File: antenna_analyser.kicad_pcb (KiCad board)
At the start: 2 copper layers, 88.9 x 53.3 mm, 25 parts, among them IC1 MCP6002, P1 CONN_01X10, P2 CONN_01X10, P3 CONN_01X04, P4 CONN_01X02

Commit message: Updates to the schematic.
Replaced 50ohm and 5kohm resistors with their equivalent parallel circuits.
Added an AD9850 module to the schematic for easier reference.
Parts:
- removed C1: 1uF, Capacitors_Elko_ThroughHole:Elko_vert_20x10mm_RM2.5
- removed C2, C4: 100n, Capacitors_ThroughHole:C_Disc_D3_P2.5
- removed C3, C5, C6: 10n, Capacitors_ThroughHole:C_Disc_D3_P2.5
- removed D1, D2: AA143, Diodes_ThroughHole:Diode_DO-41_SOD81_Horizontal_RM10
- removed IC1: MCP6002, Housings_SSOP:MSOP-8_3x3mm_Pitch0.65mm
- removed P1, P2: CONN_01X10, Pin_Headers:Pin_Header_Straight_1x10
- removed P3: CONN_01X04, Pin_Headers:Pin_Header_Straight_1x04
- removed P4: CONN_01X02, Pin_Headers:Pin_Header_Straight_1x02
- removed R1, R2, R3: 50, Resistors_ThroughHole:Resistor_Horizontal_RM10mm
- removed R10, R6: 5k, Resistors_ThroughHole:Resistor_Horizontal_RM10mm
- removed R11, R7: 648, Resistors_ThroughHole:Resistor_Horizontal_RM10mm
- removed R4, R8: 10k, Resistors_ThroughHole:Resistor_Horizontal_RM10mm
- removed R5, R9: 100k, Resistors_ThroughHole:Resistor_Horizontal_RM10mm
- removed SMA_E1: SMA_EDGE, sma:SMA
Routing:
- removed copper zone on B.Cu, net GND
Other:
- board outline removed

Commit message: PCB first attempt, no luck. Need to make sure the elements are on the correct side.
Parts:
- added C1: 1uF, Capacitors_Elko_ThroughHole:Elko_vert_20x10mm_RM2.5, F.Cu at (126.4, 108.0)
- added C2: 100n, Capacitors_ThroughHole:C_Disc_D3_P2.5, F.Cu at (162.6, 83.2)
- added C3: 10n, Capacitors_ThroughHole:C_Disc_D3_P2.5, F.Cu at (162.6, 79.4)
- added C4: 100n, Capacitors_ThroughHole:C_Disc_D3_P2.5, F.Cu at (144.1, 117.5)
- added C5: 10n, Capacitors_ThroughHole:C_Disc_D3_P2.5, F.Cu at (144.1, 120.7)
- added C6: 10n, Capacitors_ThroughHole:C_Disc_D3_P2.5, F.Cu at (92.1, 90.2)
- added D1: AA143, Diodes_ThroughHole:Diode_DO-41_SOD81_Horizontal_RM10, F.Cu at (168.3, 93.3)
- added D2: AA143, Diodes_ThroughHole:Diode_DO-41_SOD81_Horizontal_RM10, F.Cu at (168.3, 96.5)
- added ENC1: BI_EN11-HSM1AF15, Rotary-Encoders:BI_EN12-HS22AF30, F.Cu at (172.7, 113.7)
- added IC1: MCP6002, sop8:SOP-8, F.Cu at (143.5, 80.0)
- added IC2: ARDUINO_PRO_MINI_5V, arduino pro mini:ARDUINO_PRO_MINI, F.Cu at (149.2, 98.4)
- added P1: AD9850_CONN, dds-module-ad9850:DDS_AD9850, F.Cu at (109.9, 97.8)
- added P2: CONN_LCD, Pin_Headers:Pin_Header_Straight_1x15, F.Cu at (83.8, 81.9)
- added R1: 100, Resistors_ThroughHole:Resistor_Horizontal_RM10mm, F.Cu at (156.2, 101.6)
- added R10: 100, Resistors_ThroughHole:Resistor_Horizontal_RM10mm, F.Cu at (130.2, 88.3)
- added R11: 648, Resistors_ThroughHole:Resistor_Horizontal_RM10mm, F.Cu at (173.4, 78.1)
- added R12: 100, Resistors_ThroughHole:Resistor_Horizontal_RM10mm, F.Cu at (127.0, 88.3)
- added R13: 10k, Resistors_ThroughHole:Resistor_Horizontal_RM10mm, F.Cu at (94.6, 81.9)
- added R14: 10k, Resistors_ThroughHole:Resistor_Horizontal_RM10mm, F.Cu at (91.4, 81.9)
- added R15: 10k, Resistors_ThroughHole:Resistor_Horizontal_RM10mm, F.Cu at (88.3, 81.9)
- added R16: 10k, Resistors_ThroughHole:Resistor_Horizontal_RM10mm, F.Cu at (88.3, 95.2)
- added R2: 100, Resistors_ThroughHole:Resistor_Horizontal_RM10mm, F.Cu at (173.4, 87.0)
- added R3: 100, Resistors_ThroughHole:Resistor_Horizontal_RM10mm, F.Cu at (156.2, 88.3)
- added R4: 10k, Resistors_ThroughHole:Resistor_Horizontal_RM10mm, F.Cu at (173.4, 90.2)
- added R5: 100k, Resistors_ThroughHole:Resistor_Horizontal_RM10mm, F.Cu at (173.4, 83.8)
- added R6: 100, Resistors_ThroughHole:Resistor_Horizontal_RM10mm, F.Cu at (173.4, 99.7)
- added R7: 648, Resistors_ThroughHole:Resistor_Horizontal_RM10mm, F.Cu at (173.4, 80.6)
- added R8: 10k, Resistors_ThroughHole:Resistor_Horizontal_RM10mm, F.Cu at (133.3, 113.0)
- added R9: 100k, Resistors_ThroughHole:Resistor_Horizontal_RM10mm, F.Cu at (133.3, 88.3)
- added SMA_E1: SMA_EDGE, SMA_EDGE:SMA_EDGE, F.Cu at (128.3, 69.2)
- added U1: AMS1117, SOT223:SOT223, F.Cu at (130.2, 100.3)
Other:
- board outline added: 99.7 x 50.8 mm

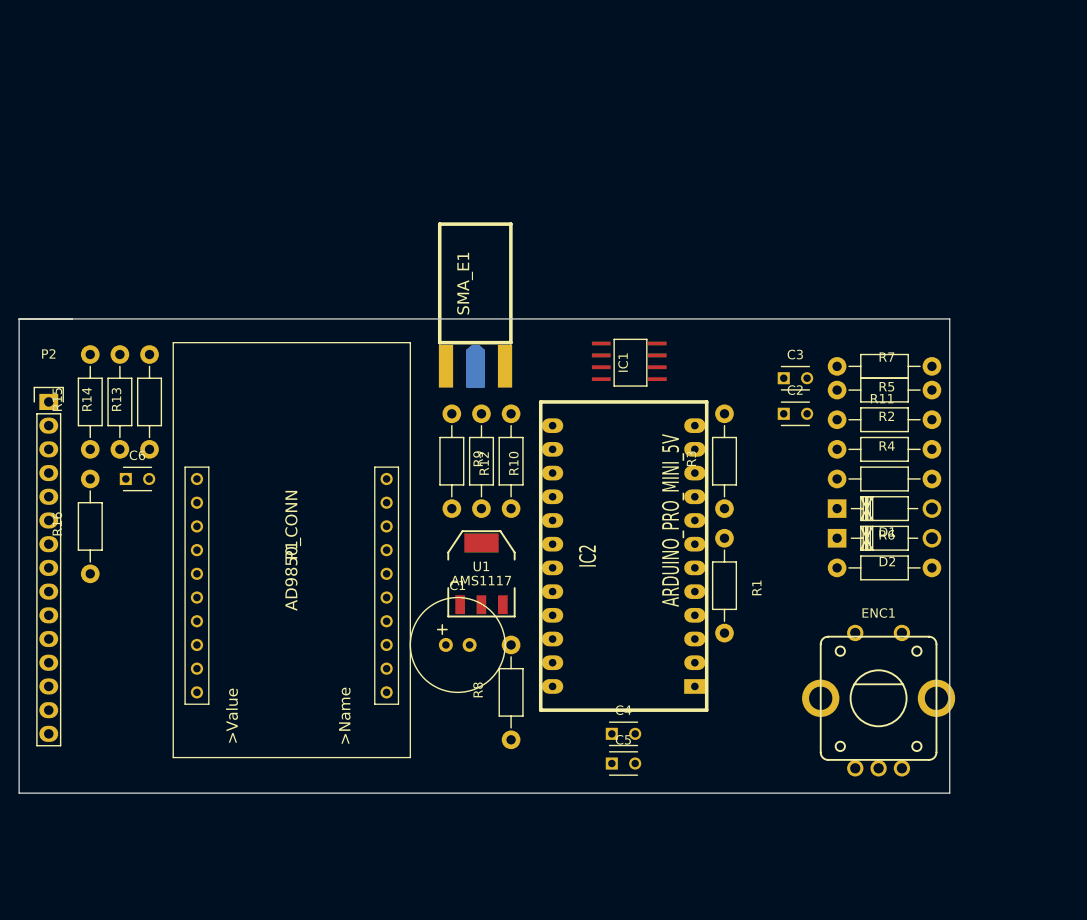
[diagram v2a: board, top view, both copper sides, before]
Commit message: MCP6002 is now properly attached on the PCB. The arduino board is attached as well. PCB needs work to be one-sided only.
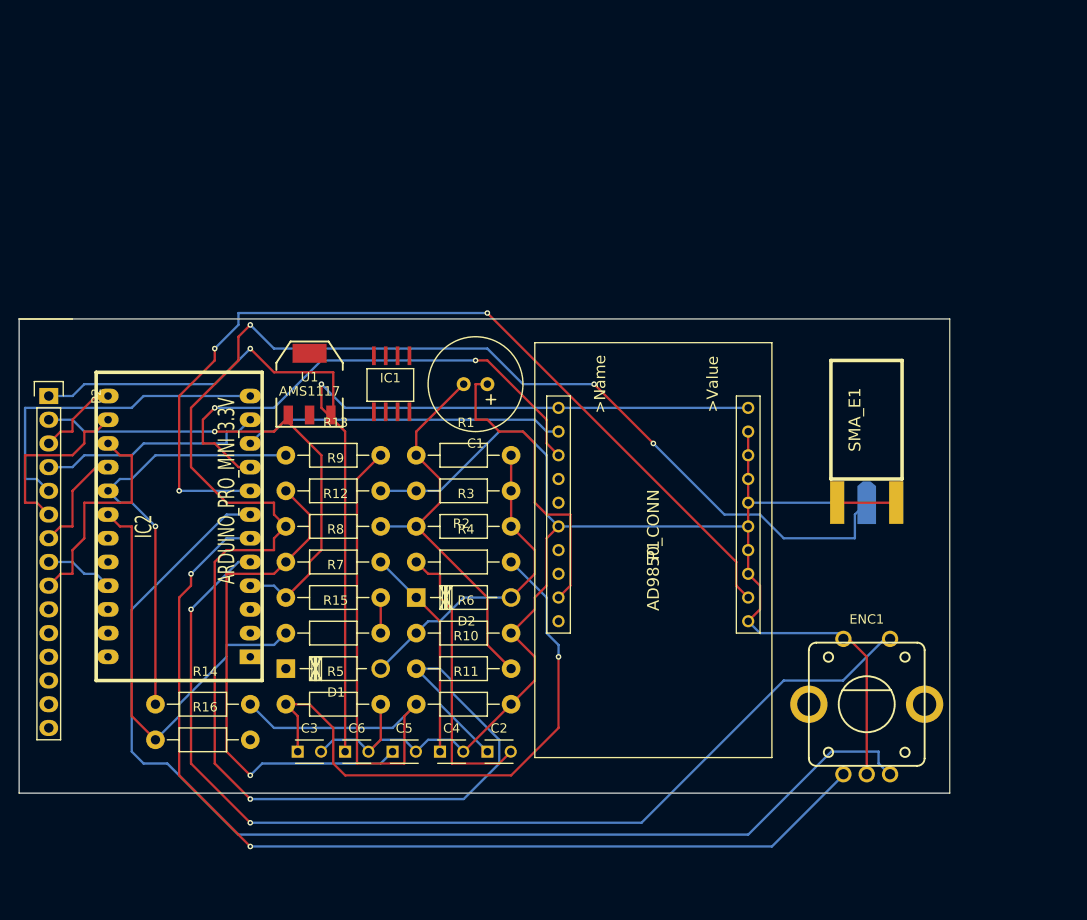
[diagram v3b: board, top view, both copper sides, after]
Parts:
- IC2: value ARDUINO_PRO_MINI_5V -> ARDUINO_PRO_MINI_3.3V
- P2: footprint Pin_Headers:Pin_Header_Straight_1x15 -> Socket_Strips:Socket_Strip_Straight_1x15
- moved R5 66.5 mm to (114.3, 114.3)
- moved C3 65.7 mm to (110.5, 119.4)
- moved R7 63.1 mm to (114.3, 102.9)
- moved D1 61.5 mm to (109.2, 110.5)
- moved R11 57.8 mm to (128.3, 114.3), turned to 0 degrees
- moved C2 48.1 mm to (130.8, 119.4)
- moved IC2 47.7 mm to (101.6, 95.2)
- moved R4 46.0 mm to (128.3, 99.1)
- moved R6 45.6 mm to (128.3, 106.7)
- moved D2 45.5 mm to (123.2, 102.9)
- moved R2 45.3 mm to (128.3, 91.4), turned to 180 degrees
- moved SMA_E1 44.4 mm to (170.2, 83.8)
- moved P1 38.7 mm to (148.6, 97.8), turned to 270 degrees
- moved C6 37.5 mm to (115.6, 119.4)
- moved R15 35.9 mm to (114.3, 106.7), turned to 0 degrees
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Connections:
- IC1 pad 1: (no net) -> Net-(IC1-Pad1)
- IC1 pad 2: (no net) -> Net-(IC1-Pad2)
- IC1 pad 3: (no net) -> Net-(C3-Pad1)
- IC1 pad 4: (no net) -> GND
- IC1 pad 5: (no net) -> Net-(C5-Pad1)
- IC1 pad 6: (no net) -> Net-(IC1-Pad6)
- IC1 pad 7: (no net) -> Net-(IC1-Pad7)
- IC1 pad 8: (no net) -> +5V
- IC2 pad 1: (no net) -> Net-(IC2-Pad1)
- IC2 pad 10: (no net) -> Net-(IC2-Pad10)
- IC2 pad 11: (no net) -> Net-(IC2-Pad11)
- IC2 pad 12: (no net) -> Net-(IC2-Pad12)
- IC2 pad 13: (no net) -> Net-(IC2-Pad13)
- IC2 pad 14: (no net) -> Net-(IC2-Pad14)
- IC2 pad 15: (no net) -> Net-(IC2-Pad15)
- IC2 pad 16: (no net) -> Net-(IC2-Pad16)
- IC2 pad 17: (no net) -> Net-(IC1-Pad7)
- IC2 pad 18: (no net) -> Net-(IC1-Pad1)
- IC2 pad 19: (no net) -> Net-(IC2-Pad19)
- IC2 pad 2: (no net) -> Net-(IC2-Pad2)
- IC2 pad 20: (no net) -> Net-(IC2-Pad20)
- IC2 pad 21: (no net) -> Net-(IC2-Pad21)
- IC2 pad 22: (no net) -> Net-(IC2-Pad22)
- IC2 pad 23: (no net) -> Net-(IC2-Pad23)
- IC2 pad 24: (no net) -> Net-(IC2-Pad24)
- IC2 pad 3: (no net) -> Net-(IC2-Pad3)
- IC2 pad 4: (no net) -> GND
- IC2 pad 5: (no net) -> Net-(ENC1-PadSW2)
- IC2 pad 6: (no net) -> Net-(ENC1-PadA)
- IC2 pad 7: (no net) -> Net-(ENC1-PadB)
- IC2 pad 8: (no net) -> Net-(IC2-Pad8)
- IC2 pad 9: (no net) -> Net-(IC2-Pad9)
- P1 pad 12: Net-(IC2-Pad~) -> Net-(IC2-Pad8)
- P1 pad 2: Net-(IC2-Pad~) -> Net-(IC2-Pad10)
- P1 pad 3: Net-(IC2-Pad~) -> Net-(IC2-Pad9)
- P2 pad 3: Net-(IC2-Pad~) -> Net-(IC2-Pad13)
- P2 pad 4: Net-(IC2-Pad~) -> Net-(IC2-Pad11)
- P2 pad 5: Net-(IC2-Pad~) -> Net-(IC2-Pad12)
- P2 pad 6: Net-(IC2-Pad~) -> Net-(IC2-Pad14)
- P2 pad 7: Net-(IC2-Pad~) -> Net-(IC2-Pad16)
- P2 pad 8: Net-(IC2-Pad~) -> Net-(IC2-Pad21)
- P2 pad 9: Net-(IC2-Pad~) -> Net-(IC2-Pad15)
- R11 pad 1: Net-(IC1-Pad~) -> Net-(IC1-Pad6)
- R13 pad 1: Net-(IC1-Pad~) -> Net-(IC1-Pad7)
- R13 pad 2: Net-(IC1-Pad~) -> Net-(IC1-Pad6)
- R14 pad 1: Net-(IC1-Pad~) -> Net-(IC1-Pad7)
- R14 pad 2: Net-(IC1-Pad~) -> Net-(IC1-Pad6)
- R15 pad 1: Net-(IC1-Pad~) -> Net-(IC1-Pad1)
- R15 pad 2: Net-(IC1-Pad~) -> Net-(IC1-Pad2)
- R16 pad 1: Net-(IC1-Pad~) -> Net-(IC1-Pad1)
- R16 pad 2: Net-(IC1-Pad~) -> Net-(IC1-Pad2)
- R7 pad 2: Net-(IC1-Pad~) -> Net-(IC1-Pad2)
- U1 pad 2: Net-(IC2-Pad~) -> Net-(IC2-Pad21)
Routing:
- net GND: track 0.00 -> 225.4 mm, vias 0 -> 1
- net Net-(C2-Pad1): track 0.00 -> 202.8 mm, vias 0 -> 4
- net +5V: track 0.00 -> 127.6 mm, vias 0 -> 2
- net Net-(ENC1-PadB): track 0.00 -> 122.7 mm
- net Net-(ENC1-PadSW2): track 0.00 -> 111.6 mm, vias 0 -> 2
- net Net-(ENC1-PadA): track 0.00 -> 107.6 mm, vias 0 -> 2
- net Net-(IC2-Pad8): track 0.00 -> 98.0 mm, vias 0 -> 3
- net Net-(IC1-Pad6): track 0.00 -> 65.9 mm
- net Net-(C3-Pad1): track 0.00 -> 62.2 mm, vias 0 -> 1
- net Net-(C5-Pad1): track 0.00 -> 55.5 mm, vias 0 -> 1
- net Net-(IC2-Pad9): track 0.00 -> 55.1 mm, vias 0 -> 2
- net Net-(IC1-Pad1): track 0.00 -> 47.2 mm
- net Net-(IC1-Pad7): track 0.00 -> 46.3 mm, vias 0 -> 1
- net Net-(C1-Pad2): track 0.00 -> 42.7 mm
- net Net-(IC2-Pad12): track 0.00 -> 35.3 mm
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
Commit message: WIP
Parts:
- removed SMA_E1: SMA_EDGE, SMA_EDGE:SMA_EDGE
- added P4: BNC, Wire_Pads:SolderWirePad_2x_1mmDrill, F.Cu at (180.3, 105.4)
- moved R9 58.2 mm to (161.3, 125.7)
- moved C5 56.6 mm to (176.5, 110.5)
- moved R14 55.1 mm to (153.7, 100.3)
- moved C1 54.5 mm to (105.4, 128.3), turned to 0 degrees
- moved R12 53.4 mm to (167.6, 92.7), turned to 180 degrees
- moved R16 53.4 mm to (153.7, 115.6)
- moved R5 52.8 mm to (166.4, 105.4), turned to 90 degrees
- moved R8 49.6 mm to (152.4, 130.8), turned to 180 degrees
- moved R15 49.1 mm to (162.6, 115.6), turned to 270 degrees
- moved R10 44.9 mm to (167.6, 88.9), turned to 180 degrees
- moved C2 44.4 mm to (168.9, 96.5), turned to 180 degrees
- moved IC1 44.2 mm to (152.4, 105.4)
- moved R7 42.7 mm to (153.7, 119.4)
- moved C3 41.0 mm to (151.1, 124.5), turned to 270 degrees
- moved C6 39.7 mm to (146.1, 94.0), turned to 270 degrees
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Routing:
- net GND: track 225.4 -> 0.00 mm, vias 1 -> 0
- net Net-(C2-Pad1): track 202.8 -> 0.00 mm, vias 4 -> 0
- net +5V: track 127.6 -> 0.00 mm, vias 2 -> 0
- net Net-(ENC1-PadB): track 122.7 -> 0.00 mm
- net Net-(ENC1-PadSW2): track 111.6 -> 0.00 mm, vias 2 -> 0
- net Net-(ENC1-PadA): track 107.6 -> 0.00 mm, vias 2 -> 0
- net Net-(IC2-Pad8): track 98.0 -> 0.00 mm, vias 3 -> 0
- net Net-(IC1-Pad6): track 65.9 -> 0.00 mm
- net Net-(C3-Pad1): track 62.2 -> 0.00 mm, vias 1 -> 0
- net Net-(C5-Pad1): track 55.5 -> 0.00 mm, vias 1 -> 0
- net Net-(IC2-Pad9): track 55.1 -> 0.00 mm, vias 2 -> 0
- net Net-(IC1-Pad1): track 47.2 -> 0.00 mm
- net Net-(IC1-Pad7): track 46.3 -> 0.00 mm, vias 1 -> 0
- net Net-(C1-Pad2): track 42.7 -> 0.00 mm
- net Net-(IC2-Pad12): track 35.3 -> 0.00 mm
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- added copper zone on F.Cu, net GND
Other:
- board size 99.7 x 50.8 mm -> 100 x 50 mm

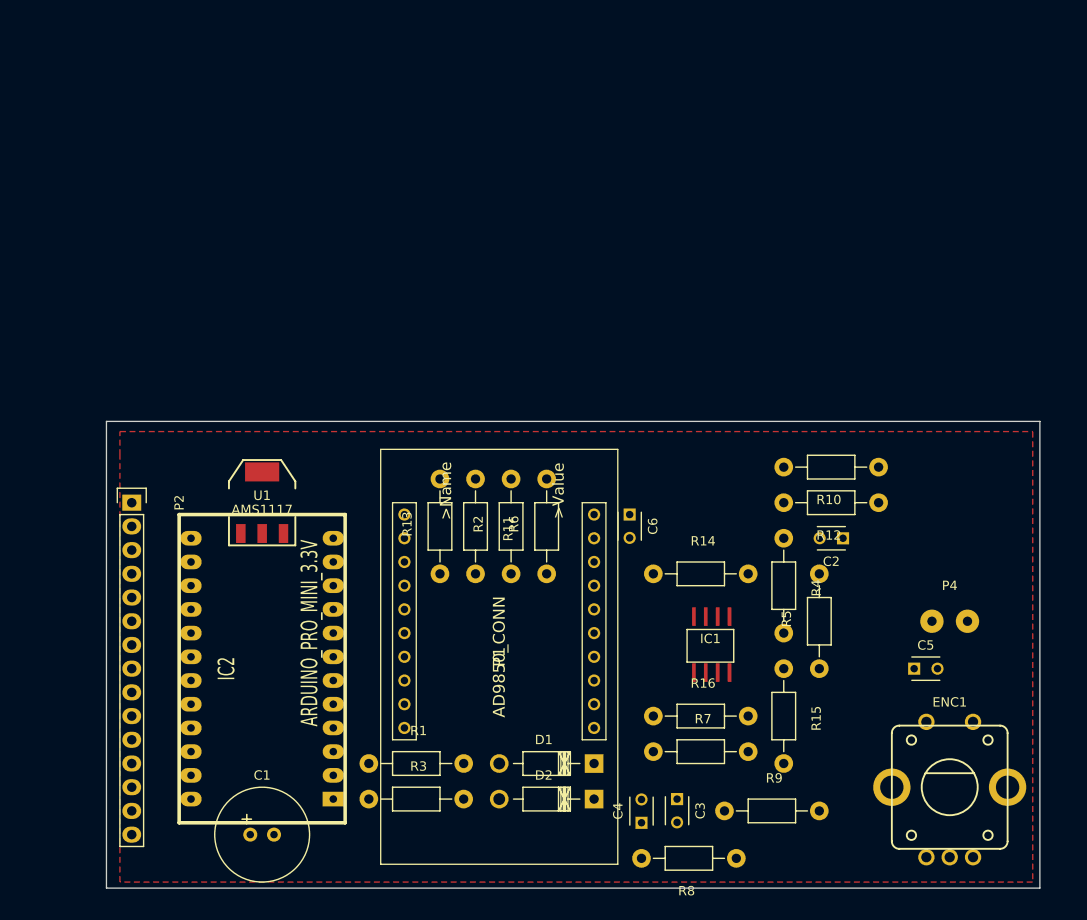
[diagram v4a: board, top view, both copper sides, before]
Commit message: Playing with freerouting, need to lay components according to a semi-planar schema and run freerouting on it.
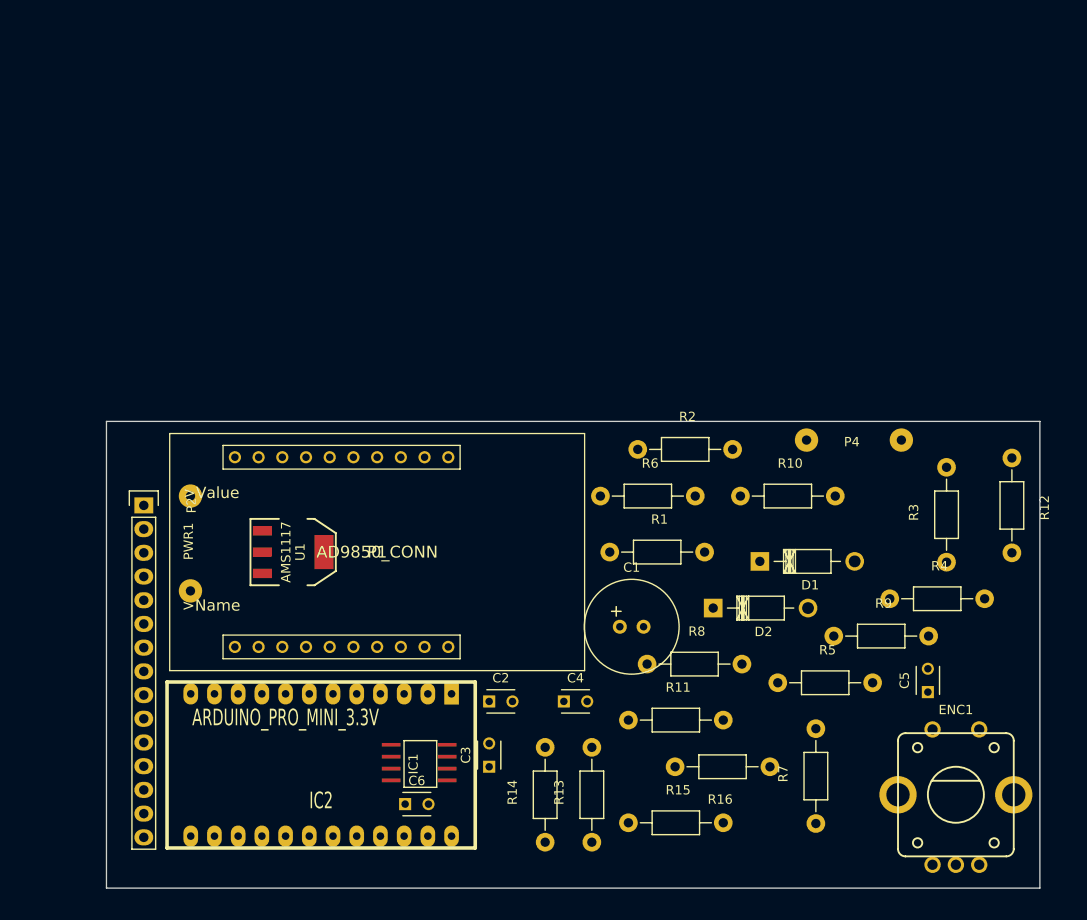
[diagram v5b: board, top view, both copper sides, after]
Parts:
- added PWR1: CONN_01X02, Wire_Connections_Bridges:WireConnection_1mmDrill, F.Cu at (99.0, 92.0)
- P4: footprint Wire_Pads:SolderWirePad_2x_1mmDrill -> Wire_Connections_Bridges:WireConnection_1mmDrill
- moved R3 64.5 mm to (180.0, 94.0), turned to 90 degrees
- moved C1 45.4 mm to (145.0, 106.0)
- moved C2 41.7 mm to (131.0, 114.0), turned to 0 degrees
- moved C6 39.3 mm to (122.0, 125.0), turned to 0 degrees
- moved IC1 36.0 mm to (121.0, 123.0), turned to 90 degrees
- moved R1 34.3 mm to (149.0, 98.0)
- moved R13 33.0 mm to (142.0, 124.0)
- moved R11 29.9 mm to (151.0, 116.0), turned to 0 degrees
- moved R14 29.0 mm to (137.0, 124.0), turned to 90 degrees
- moved D1 28.0 mm to (160.0, 99.0), turned to 0 degrees
- moved P4 24.7 mm to (165.0, 86.0)
- moved D2 24.1 mm to (155.0, 104.0), turned to 0 degrees
- moved R9 22.1 mm to (173.0, 107.0)
- moved R8 20.8 mm to (153.0, 110.0), turned to 0 degrees
- moved C3 20.4 mm to (131.0, 121.0), turned to 90 degrees
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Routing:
- removed copper zone on F.Cu, net GND
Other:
- net class Default: clearance 0.2 -> 0.3; trace_width 0.25 -> 0.3
- rule trace_clearance: 0.2 -> 0.3

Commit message: Moving some components around so that freerouting can produce a single sided PCB.
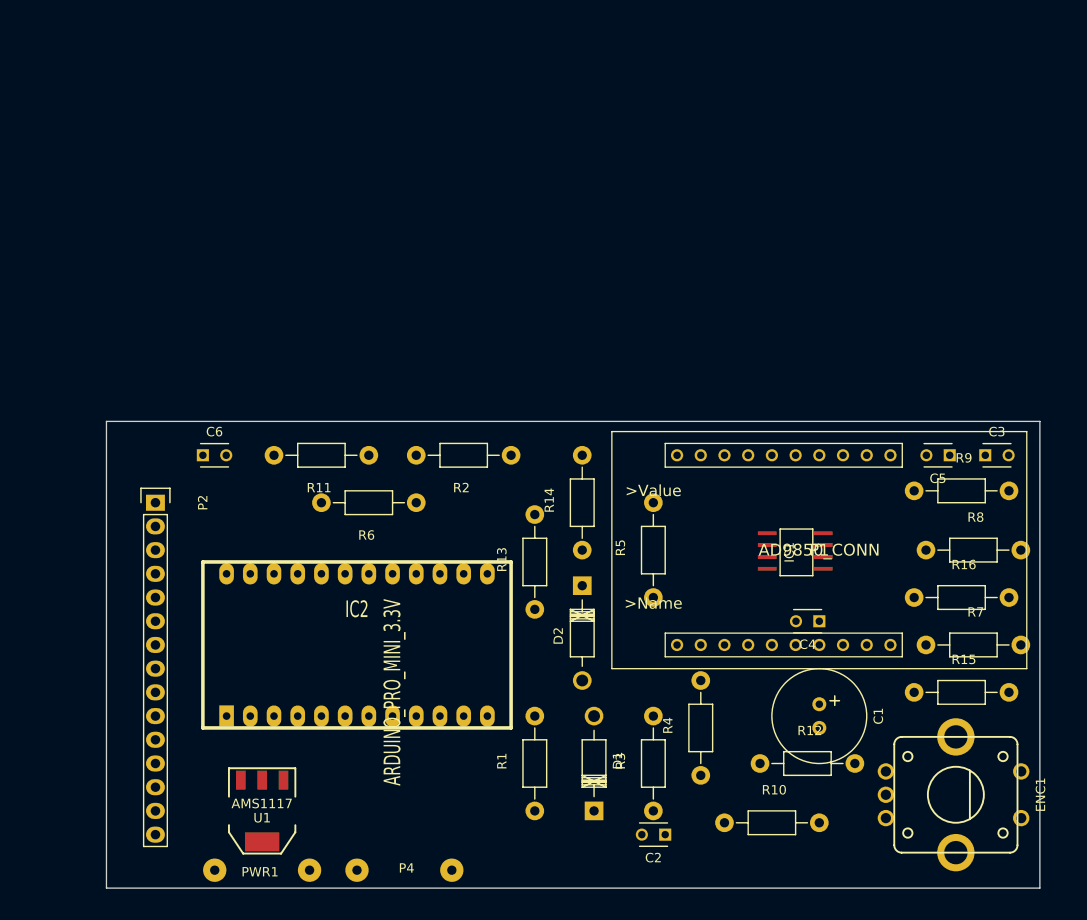
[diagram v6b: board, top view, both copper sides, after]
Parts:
- moved C3 62.8 mm to (184.2, 87.6), turned to 0 degrees
- moved P4 59.7 mm to (127.0, 132.1), turned to 180 degrees
- moved R11 47.4 mm to (113.0, 87.6), turned to 180 degrees
- moved P1 47.4 mm to (166.4, 97.8)
- moved IC1 46.2 mm to (161.3, 100.3)
- moved C6 43.2 mm to (100.3, 87.6)
- moved R3 41.2 mm to (148.6, 120.7)
- moved PWR1 40.2 mm to (101.6, 132.1), turned to 0 degrees
- moved R12 35.3 mm to (165.1, 120.7), turned to 0 degrees
- moved R10 35.0 mm to (161.3, 127.0)
- moved R15 33.6 mm to (181.6, 113.0)
- moved R8 32.3 mm to (182.9, 97.8)
- moved D1 32.1 mm to (142.2, 125.7), turned to 90 degrees
- moved R14 31.5 mm to (141.0, 92.7)
- moved R16 31.4 mm to (181.6, 102.9), turned to 0 degrees
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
